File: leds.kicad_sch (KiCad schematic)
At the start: 61 parts, among them U16 ADUM1201ARZ-RL7

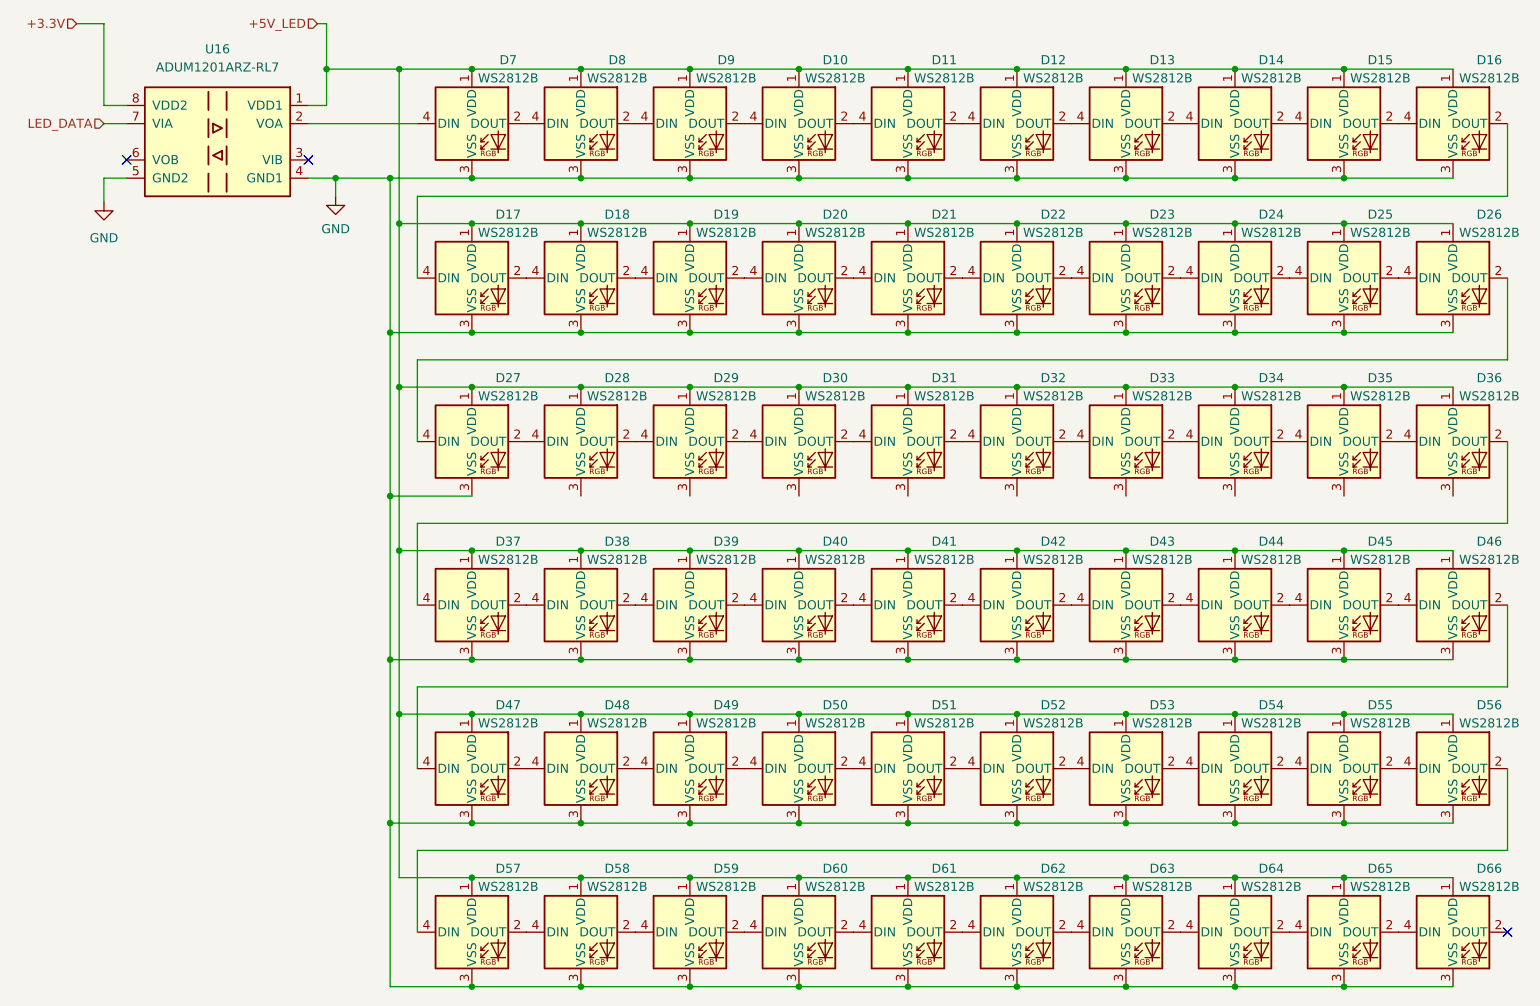
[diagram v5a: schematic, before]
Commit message: replaced main MCU, reannotated
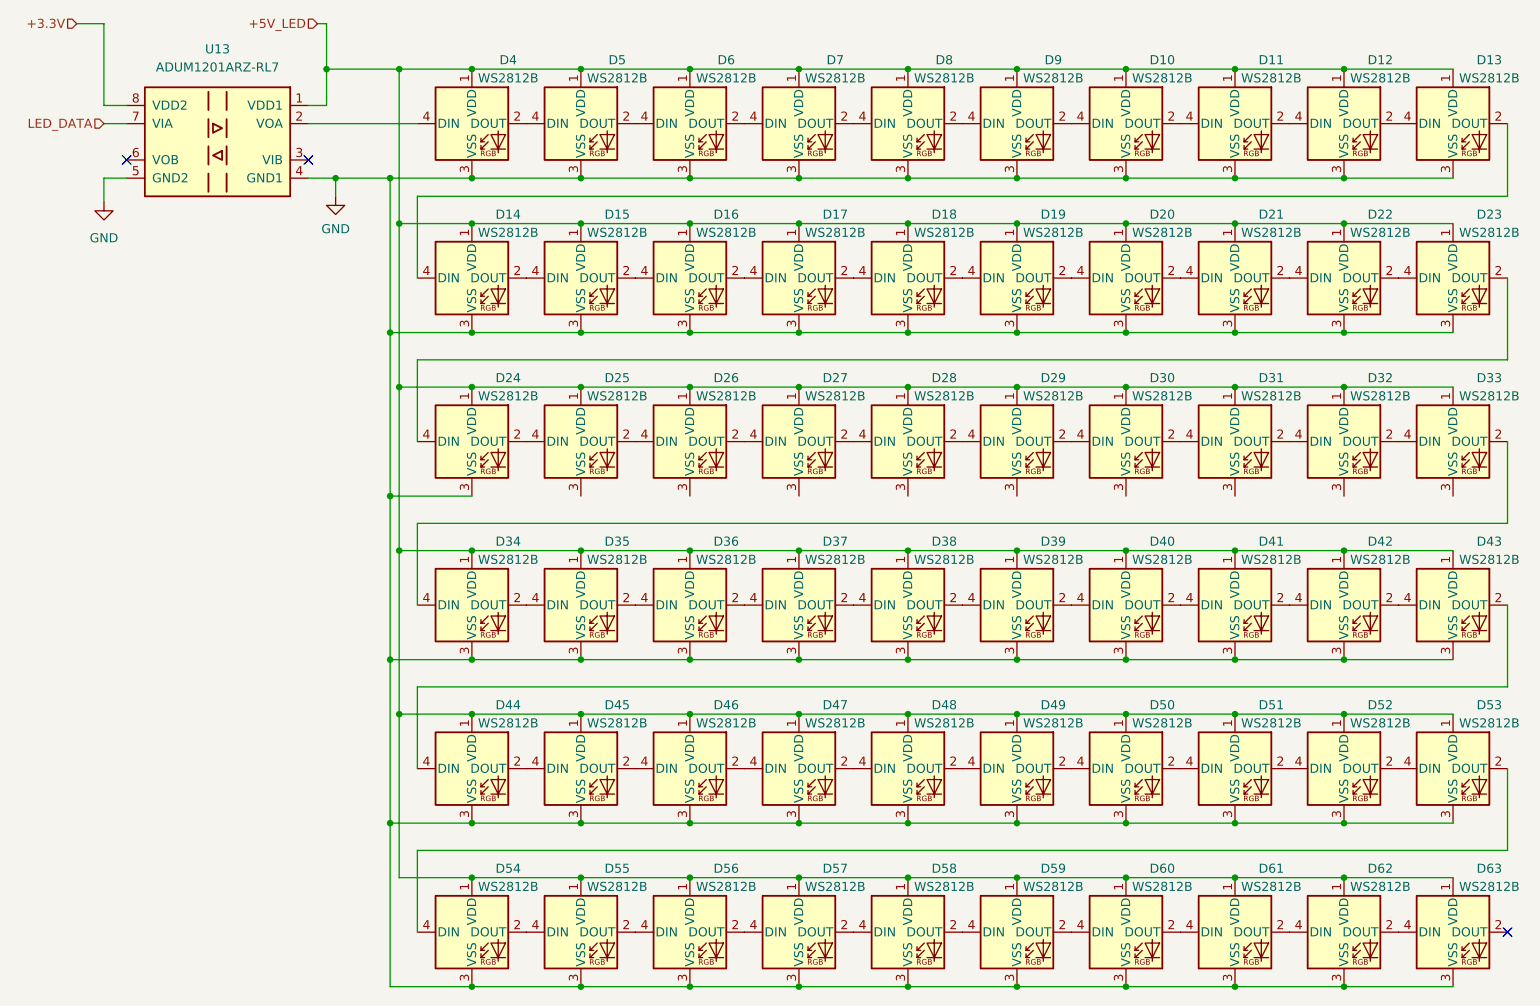
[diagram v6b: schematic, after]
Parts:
- renumbered D13 to D10, D14 to D11, D15 to D12, D16 to D13, D17 to D14, D18 to D15, D19 to D16, D20 to D17, D21 to D18, D22 to D19, D23 to D20, D24 to D21, D25 to D22, D26 to D23, D27 to D24, D28 to D25, D29 to D26, D30 to D27, D31 to D28, D32 to D29, D33 to D30, D34 to D31, D35 to D32, D36 to D33, D37 to D34, D38 to D35, D39 to D36, D40 to D37, D41 to D38, D42 to D39, D7 to D4, D43 to D40, D44 to D41, D45 to D42, D46 to D43, D47 to D44, D48 to D45, D49 to D46, D50 to D47, D51 to D48, D52 to D49, D8 to D5, D53 to D50, D54 to D51, D55 to D52, D56 to D53, D57 to D54, D58 to D55, D59 to D56, D60 to D57, D61 to D58, D62 to D59, D9 to D6, D63 to D60, D64 to D61, D65 to D62, D66 to D63, D10 to D7, D11 to D8, D12 to D9, U16 to U13

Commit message: resolved all erc errors
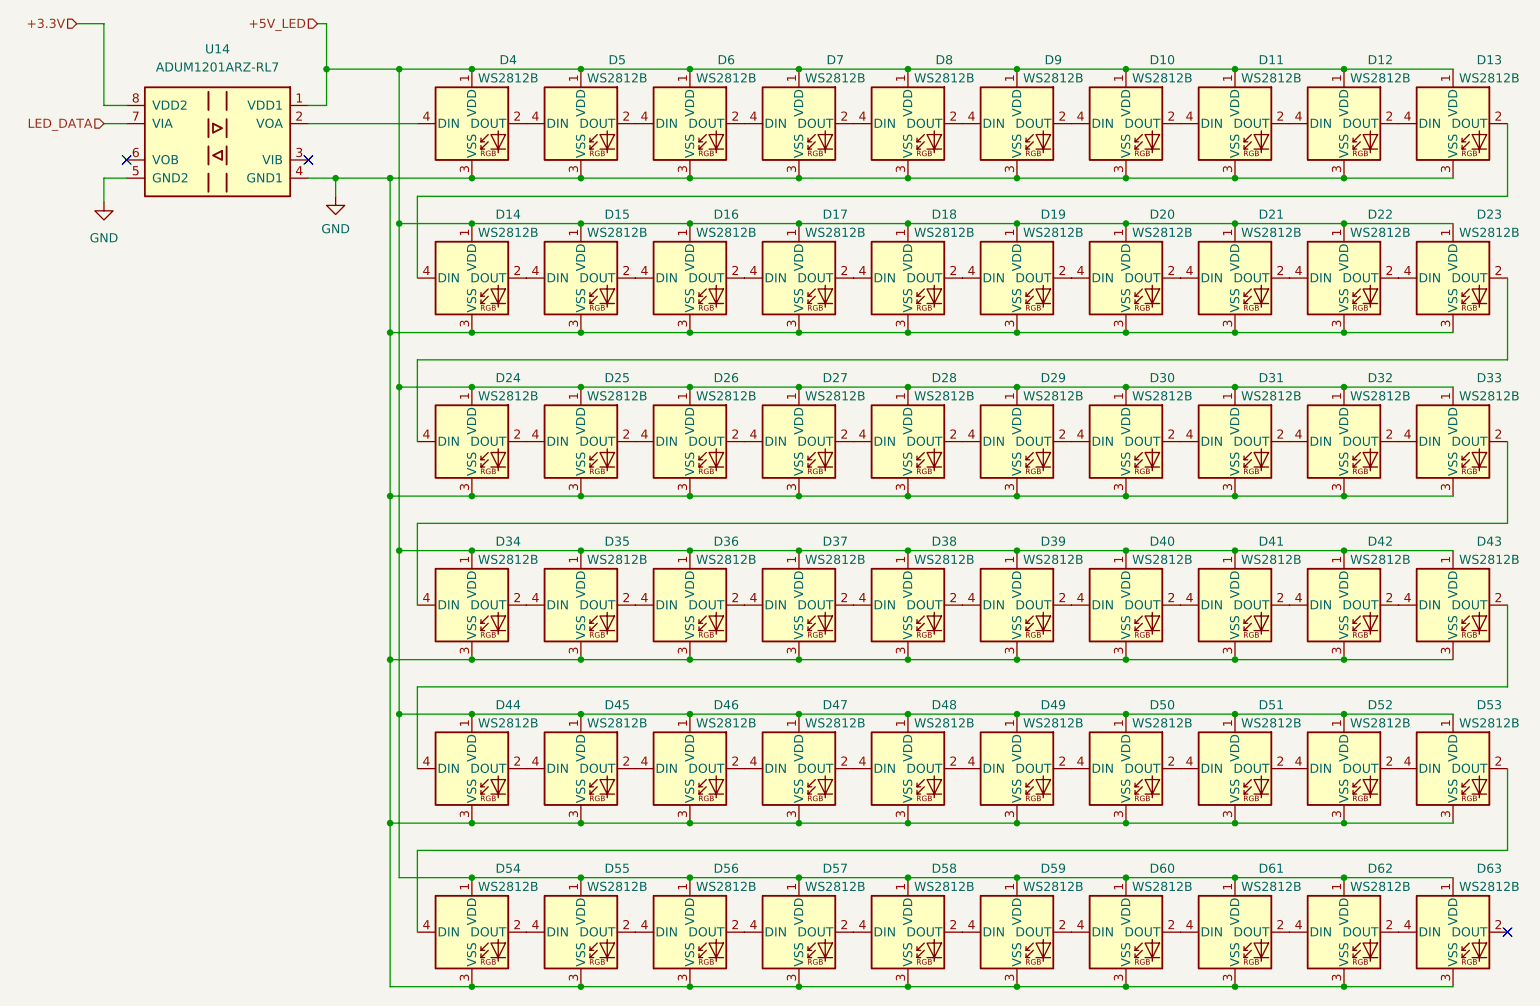
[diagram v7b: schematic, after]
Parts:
- renumbered U13 to U14
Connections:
- net GND: now also D25.3 (VSS), D26.3 (VSS), D27.3 (VSS), D28.3 (VSS), D29.3 (VSS), D30.3 (VSS), D31.3 (VSS), D32.3 (VSS), D33.3 (VSS)
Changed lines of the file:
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@@
   (junction (at 113.03 125.73) (diameter 0) (color 0 0 0 0)
   )
+  (junction (at 204.47 95.25) (diameter 0) (color 0 0 0 0)
+  )
   (junction (at 128.27 50.8) (diameter 0) (color 0 0 0 0)
   )
+  (junction (at 128.27 95.25) (diameter 0) (color 0 0 0 0)
+  )
   (junction (at 86.36 140.97) (diameter 0) (color 0 0 0 0)
   )
@@
   (junction (at 87.63 125.73) (diameter 0) (color 0 0 0 0)
   )
+  (junction (at 189.23 95.25) (diameter 0) (color 0 0 0 0)
+  )
   (junction (at 97.79 118.11) (diameter 0) (color 0 0 0 0)
   )
+  (junction (at 143.51 95.25) (diameter 0) (color 0 0 0 0)
+  )
   (junction (at 97.79 140.97) (diameter 0) (color 0 0 0 0)
   )
@@
   (junction (at 143.51 163.83) (diameter 0) (color 0 0 0 0)
   )
+  (junction (at 113.03 95.25) (diameter 0) (color 0 0 0 0)
+  )
   (junction (at 143.51 125.73) (diameter 0) (color 0 0 0 0)
   )
@@
   (junction (at 97.79 35.56) (diameter 0) (color 0 0 0 0)
   )
+  (junction (at 158.75 95.25) (diameter 0) (color 0 0 0 0)
+  )
+  (junction (at 97.79 95.25) (diameter 0) (color 0 0 0 0)
+  )
   (junction (at 219.71 35.56) (diameter 0) (color 0 0 0 0)
   )
@@
   (junction (at 128.27 163.83) (diameter 0) (color 0 0 0 0)
   )
+  (junction (at 219.71 95.25) (diameter 0) (color 0 0 0 0)
+  )
   (junction (at 219.71 57.15) (diameter 0) (color 0 0 0 0)
   )
@@
   )
   (junction (at 97.79 125.73) (diameter 0) (color 0 0 0 0)
+  )
+  (junction (at 173.99 95.25) (diameter 0) (color 0 0 0 0)
   )
   (junction (at 113.03 35.56) (diameter 0) (color 0 0 0 0)
@@
     (stroke (width 0) (type default) (color 0 0 0 0))
   )
+  (wire (pts (xy 143.51 95.25) (xy 158.75 95.25))
+    (stroke (width 0) (type default) (color 0 0 0 0))
+  )
   (wire (pts (xy 242.57 43.18) (xy 242.57 53.34))
     (stroke (width 0) (type default) (color 0 0 0 0))
@@
     (stroke (width 0) (type default) (color 0 0 0 0))
   )
+  (wire (pts (xy 204.47 95.25) (xy 219.71 95.25))
+    (stroke (width 0) (type default) (color 0 0 0 0))
+  )
   (wire (pts (xy 97.79 125.73) (xy 113.03 125.73))
     (stroke (width 0) (type default) (color 0 0 0 0))
@@
     (stroke (width 0) (type default) (color 0 0 0 0))
   )
+  (wire (pts (xy 113.03 95.25) (xy 128.27 95.25))
+    (stroke (width 0) (type default) (color 0 0 0 0))
+  )
   (wire (pts (xy 143.51 72.39) (xy 158.75 72.39))
     (stroke (width 0) (type default) (color 0 0 0 0))
@@
     (stroke (width 0) (type default) (color 0 0 0 0))
   )
+  (wire (pts (xy 128.27 95.25) (xy 143.51 95.25))
+    (stroke (width 0) (type default) (color 0 0 0 0))
+  )
   (wire (pts (xy 158.75 35.56) (xy 173.99 35.56))
     (stroke (width 0) (type default) (color 0 0 0 0))
@@
     (stroke (width 0) (type default) (color 0 0 0 0))
   )
+  (wire (pts (xy 219.71 95.25) (xy 234.95 95.25))
+    (stroke (width 0) (type default) (color 0 0 0 0))
+  )
   (wire (pts (xy 97.79 50.8) (xy 113.03 50.8))
     (stroke (width 0) (type default) (color 0 0 0 0))
@@
     (stroke (width 0) (type default) (color 0 0 0 0))
   )
+  (wire (pts (xy 189.23 95.25) (xy 204.47 95.25))
+    (stroke (width 0) (type default) (color 0 0 0 0))
+  )
   (wire (pts (xy 189.23 140.97) (xy 204.47 140.97))
     (stroke (width 0) (type default) (color 0 0 0 0))
@@
     (stroke (width 0) (type default) (color 0 0 0 0))
   )
+  (wire (pts (xy 97.79 95.25) (xy 113.03 95.25))
+    (stroke (width 0) (type default) (color 0 0 0 0))
+  )
   (wire (pts (xy 158.75 80.01) (xy 173.99 80.01))
     (stroke (width 0) (type default) (color 0 0 0 0))
@@
     (stroke (width 0) (type default) (color 0 0 0 0))
   )
+  (wire (pts (xy 173.99 95.25) (xy 189.23 95.25))
+    (stroke (width 0) (type default) (color 0 0 0 0))
+  )
   (wire (pts (xy 97.79 80.01) (xy 113.03 80.01))
     (stroke (width 0) (type default) (color 0 0 0 0))
@@
   )
   (wire (pts (xy 87.63 125.73) (xy 87.63 148.59))
+    (stroke (width 0) (type default) (color 0 0 0 0))
+  )
+  (wire (pts (xy 158.75 95.25) (xy 173.99 95.25))
     (stroke (width 0) (type default) (color 0 0 0 0))
   )
@@
   (symbol (lib_id "power:GND") (at 46.355 54.102 0) (mirror y) (unit 1)
     (in_bom yes) (on_board yes) (fields_autoplaced)
-    (property "Reference" "#PWR098" (id 0) (at 46.355 60.452 0)
+    (property "Reference" "#PWR092" (id 0) (at 46.355 60.452 0)
       (effects (font (size 1.27 1.27)) hide)
     )
@@
   (symbol (lib_id "power:GND") (at 78.74 53.34 0) (mirror y) (unit 1)
     (in_bom yes) (on_board yes) (fields_autoplaced)
-    (property "Reference" "#PWR097" (id 0) (at 78.74 59.69 0)
+    (property "Reference" "#PWR091" (id 0) (at 78.74 59.69 0)
       (effects (font (size 1.27 1.27)) hide)
     )
@@
   (symbol (lib_id "Isolator:ADuM1201AR") (at 62.23 45.72 0) (mirror y) (unit 1)
     (in_bom yes) (on_board yes) (fields_autoplaced)
-    (property "Reference" "U13" (id 0) (at 62.23 32.766 0))
+    (property "Reference" "U14" (id 0) (at 62.23 32.766 0))
     (property "Value" "ADUM1201ARZ-RL7" (id 1) (at 62.23 35.306 0))
     (property "Footprint" "Package_SO:SOIC-8_3.9x4.9mm_P1.27mm" (id 2) (at 62.23 55.88 0)

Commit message: updated footprints from schematics
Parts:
- D10, D11, D12, D13, D14, D15, D16, D17, D18, D19, D20, D21, D22, D23, D24, D25, D26, D27, D28, D29, D30, D31, D32, D33, D34, D35, D36, D37, D38, D39, D4, D40, D41, D42, D43, D44, D45, D46, D47, D48, D49, D5, D50, D51, D52, D53, D54, D55, D56, D57, D58, D59, D6, D60, D61, D62, D63, D7, D8, D9: footprint LED_SMD:LED_WS2812B_PLCC4_5.0x5.0mm_P3.2mm -> Robotont:LED3535
